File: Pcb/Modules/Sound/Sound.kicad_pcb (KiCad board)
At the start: 2 copper layers, 15 parts, among them J1 JACK_RJ45, U1 MAX4466

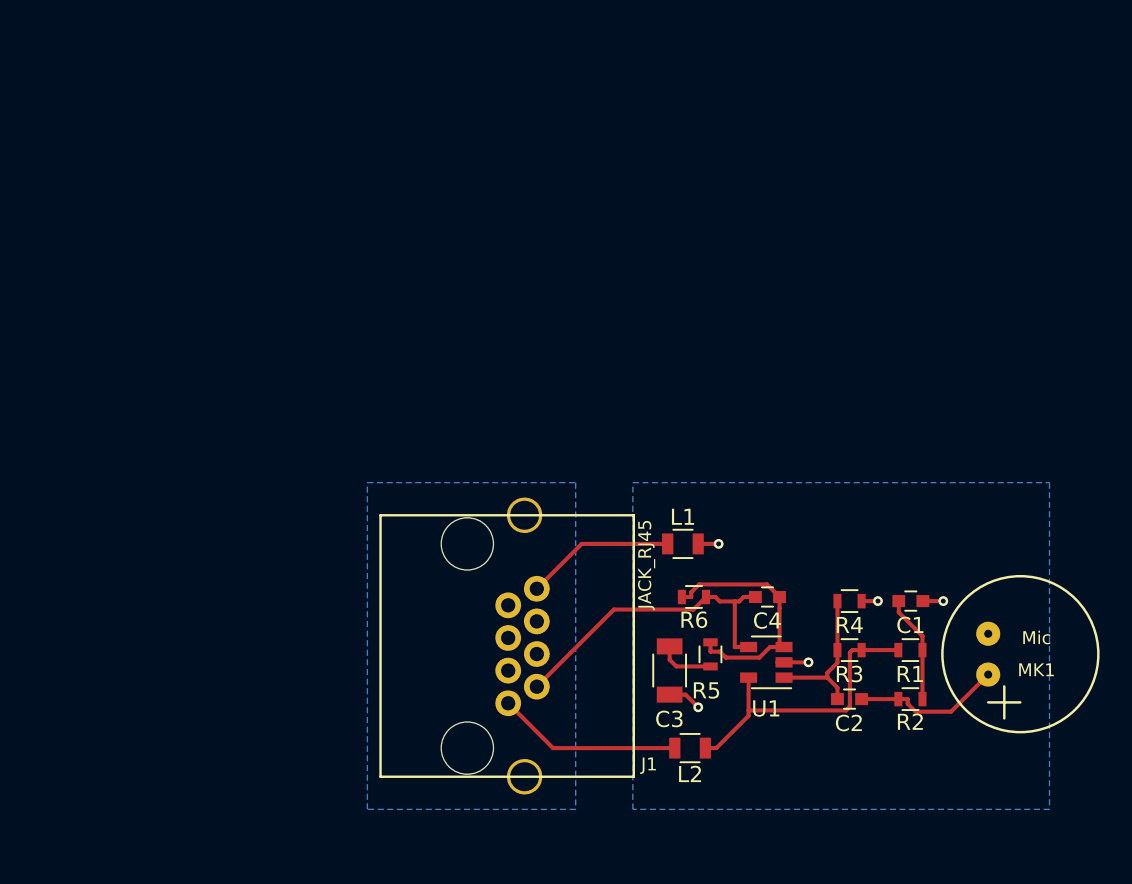
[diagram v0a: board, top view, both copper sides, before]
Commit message: Update module pcbs to common format and fix issues.
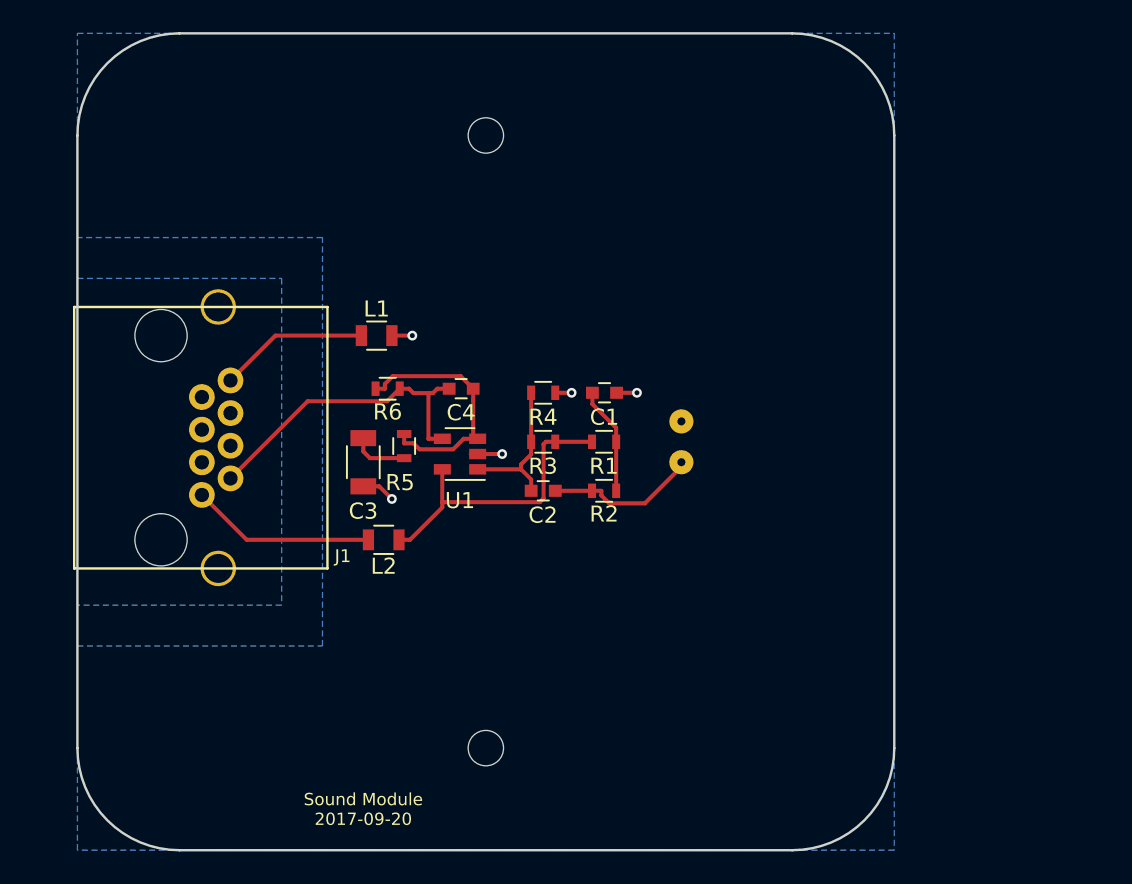
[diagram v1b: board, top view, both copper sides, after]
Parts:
- added REF**: MountingHole_2.2mm_M2, Mounting_Holes:MountingHole_2.2mm_M2, F.Cu at (50.8, 69.8)
- added REF**: MountingHole_2.2mm_M2, Mounting_Holes:MountingHole_2.2mm_M2, F.Cu at (50.8, 31.8)
- MK1: moved to B.Cu
- moved MK1 26.6 mm to (61.0, 50.8), turned to 0 degrees
- moved C2 23.0 mm to (54.4, 53.8)
- moved U1 23.0 mm to (49.2, 51.6)
- moved R3 23.0 mm to (54.4, 50.8)
- moved R4 23.0 mm to (54.4, 47.8)
- moved C1 23.0 mm to (58.2, 47.8)
- moved C3 23.0 mm to (43.2, 52.1)
- moved J1 23.0 mm to (33.0, 50.5)
- moved L1 23.0 mm to (44.0, 44.2)
- moved R2 23.0 mm to (58.2, 53.8)
- moved R6 23.0 mm to (44.7, 47.5)
- moved C4 23.0 mm to (49.3, 47.5)
- moved L2 23.0 mm to (44.5, 56.9)
- moved R1 23.0 mm to (58.2, 50.8)
- moved R5 23.0 mm to (45.7, 51.1)
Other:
- board outline added: 50.8 x 50.8 mm
- net class Default: clearance 0.2032 -> 0.2; trace_width 0.254 -> 0.25; via_dia 0.6096 -> 0.6; via_drill 0.3048 -> 0.4
- rule trace_clearance: 0.2032 -> 0.2
- board text added: "Sound Module 2017-09-20"

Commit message: Update sound module
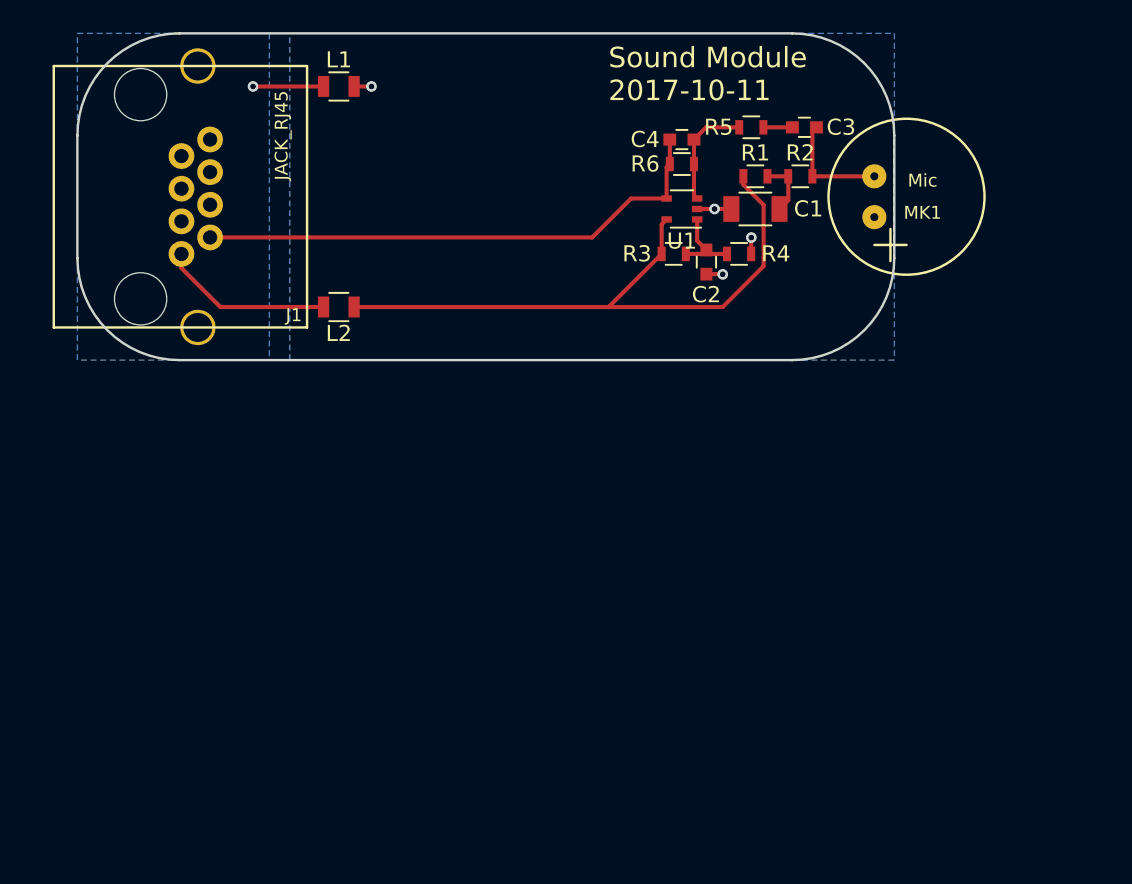
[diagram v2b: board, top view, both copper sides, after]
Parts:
- removed REF** (x2): MountingHole_2.2mm_M2, Mounting_Holes:MountingHole_2.2mm_M2
- C1: value 0.1uF -> 47uF; footprint Capacitors_SMD:C_0603 -> Capacitors_SMD:C_1206
- C2: value 0.01uF -> 1uF
- C3: value 10uF -> 0.1uF; footprint Capacitors_SMD:C_1206 -> Capacitors_SMD:C_0603
- C4: value 100pF -> 47pF
- MK1: moved to F.Cu
- R2: value 1K -> 2.2K
- R3, R4: value 1M -> 100K
- R5: value 1K -> 20K
- R6: value 100K -> 1M
- U1: footprint TO_SOT_Packages_SMD:SOT-23-5 -> TO_SOT_Packages_SMD:SOT-353_SC-70-5
- moved C3 34.4 mm to (70.6, 31.2), turned to 180 degrees
- moved R5 29.3 mm to (67.3, 31.2), turned to 0 degrees
- moved R2 23.1 mm to (70.4, 34.3), turned to 0 degrees
- moved R6 23.0 mm to (63.0, 33.5), turned to 0 degrees
- moved MK1 22.1 mm to (77.0, 35.6), turned to 180 degrees
- moved C4 20.7 mm to (63.0, 32.0)
- moved U1 20.6 mm to (63.0, 36.3)
- moved R1 19.0 mm to (67.6, 34.3)
- moved C2 17.5 mm to (64.5, 39.6), turned to 90 degrees
- moved L1 15.7 mm to (41.7, 28.7)
- moved J1 15.0 mm to (31.8, 35.6)
- moved R4 14.9 mm to (66.5, 39.1)
- moved C1 14.8 mm to (67.6, 36.3), turned to 180 degrees
- moved L2 14.7 mm to (41.7, 42.4)
- moved R3 14.2 mm to (62.5, 39.1), turned to 0 degrees
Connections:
- C2 pad 1: Net-(C2-Pad1) -> GND
- C3 pad 1: GND -> Net-(C3-Pad1)
- MK1 pad 1: GND -> Net-(C3-Pad1)
- MK1 pad 2: Net-(C2-Pad2) -> GND
- R2 pad 2: Net-(C2-Pad2) -> Net-(C3-Pad1)
- R3 pad 2: Net-(C2-Pad1) -> Net-(C2-Pad2)
- R4 pad 1: Net-(C2-Pad1) -> Net-(C2-Pad2)
- U1 pad 1: Net-(C2-Pad1) -> Net-(C2-Pad2)
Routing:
- net +3V3: track 18.7 -> 39.6 mm
- net /AN_VAL: track 19.8 -> 33.1 mm
- net Net-(C2-Pad1): track 9.31 -> 0.00 mm
- net Net-(C4-Pad1): track 15.6 -> 6.88 mm
- net Net-(C3-Pad1): track 0.00 -> 7.01 mm
- net Net-(J1-Pad8): track 9.29 -> 4.38 mm, vias 0 -> 1
- net Net-(C2-Pad2): track 9.32 -> 4.90 mm
- net Net-(C1-Pad1): track 6.71 -> 3.55 mm
- net GND: track 7.61 -> 5.25 mm, vias 5 -> 4
- net Net-(C3-Pad2): track 3.54 -> 1.80 mm
- net Net-(J1-Pad1): track 11.5 -> 10.7 mm
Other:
- board size 50.8 x 50.8 mm -> 50.8 x 20.3 mm
- net class Default: clearance 0.2 -> 0.2032; trace_width 0.25 -> 0.254; via_dia 0.6 -> 0.6604; via_drill 0.4 -> 0.3556
- rule trace_clearance: 0.2 -> 0.2032
- board text added: "Sound Module 2017-10-11"
- board text removed: "Sound Module 2017-09-20"

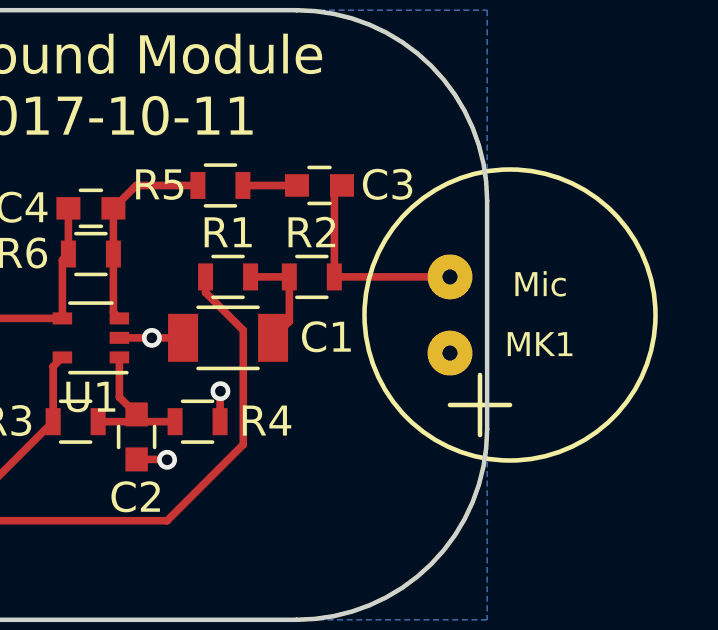
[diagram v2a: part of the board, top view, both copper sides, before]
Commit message: Update vibration module pcb
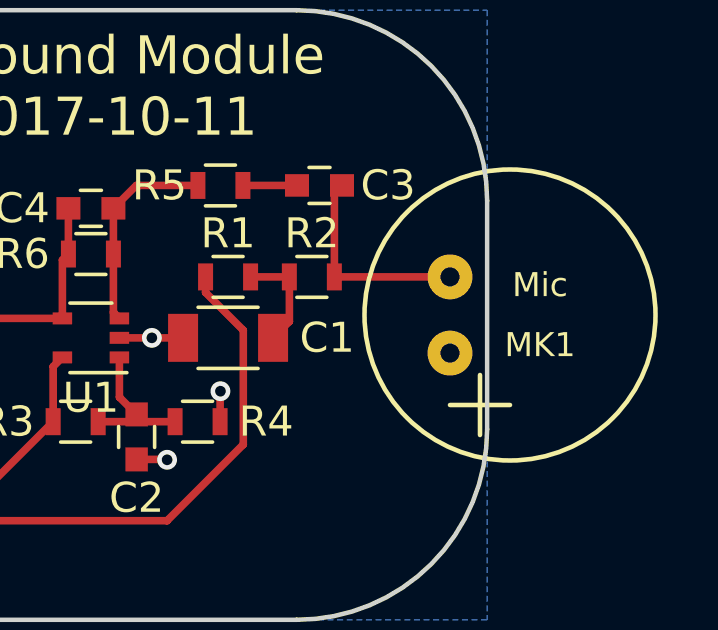
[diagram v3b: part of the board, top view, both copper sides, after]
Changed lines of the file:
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@@
     (links 26)
     (no_connects 0)
-    (area 25.324999 25.324999 76.275001 45.795001)
+    (area 23.651869 25.324999 82.091401 45.795001)
     (thickness 1.6)
     (drawings 9)
@@
     (mod_text_size 1 1)
     (mod_text_width 0.15)
-    (pad_size 1.524 1.524)
-    (pad_drill 0.762)
+    (pad_size 1.5 1.5)
+    (pad_drill 0.635)
     (pad_to_mask_clearance 0.2)
     (aux_axis_origin 0 0)
@@
     (fp_line (start 1 -4) (end 1 -2) (layer F.SilkS) (width 0.1524))
     (fp_circle (center 0 0) (end 4.85 0) (layer F.SilkS) (width 0.1524))
-    (pad 1 thru_hole circle (at 2 1.27 180) (size 1.5 1.5) (drill 0.5) (layers *.Cu *.Mask)
+    (pad 1 thru_hole circle (at 2 1.27 180) (size 1.5 1.5) (drill 0.635) (layers *.Cu *.Mask)
       (net 10 "Net-(C3-Pad1)"))
-    (pad 2 thru_hole circle (at 2 -1.27 180) (size 1.5 1.5) (drill 0.5) (layers *.Cu *.Mask)
+    (pad 2 thru_hole circle (at 2 -1.27 180) (size 1.5 1.5) (drill 0.635) (layers *.Cu *.Mask)
       (net 1 GND))
   )

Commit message: Update Valve module
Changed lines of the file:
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@@
     (add_net "Net-(J1-Pad8)")
-  )
-  (module CA6:MIC_CMA-4544PF (layer F.Cu)
-    (at 76.962 35.56 180)
-    (tags "CMS SM")
-    (attr smd)
-    (fp_text reference MK1 (at -1 -1 180) (layer F.SilkS)
-      (effects (font (size 0.8 0.8) (thickness 0.15)))
-    )
-    (fp_text value Mic (at -1 1 180) (layer F.SilkS)
-      (effects (font (size 0.8 0.8) (thickness 0.15)))
-    )
-    (fp_line (start 0 -3) (end 2 -3) (layer F.SilkS) (width 0.1524))
-    (fp_line (start 1 -4) (end 1 -2) (layer F.SilkS) (width 0.1524))
-    (fp_circle (center 0 0) (end 4.85 0) (layer F.SilkS) (width 0.1524))
-    (pad 1 thru_hole circle (at 2 1.27 180) (size 1.5 1.5) (drill 0.635) (layers *.Cu *.Mask)
-      (net 10 "Net-(C3-Pad1)"))
-    (pad 2 thru_hole circle (at 2 -1.27 180) (size 1.5 1.5) (drill 0.635) (layers *.Cu *.Mask)
-      (net 1 GND))
   )
   (module Capacitors_SMD:C_0603 (layer F.Cu)
@@
     )
   )
+  (module CA6:MIC_CMA-4544PF (layer F.Cu)
+    (at 76.962 35.56 180)
+    (tags "CMS SM")
+    (attr smd)
+    (fp_text reference MK1 (at -1 -1 180) (layer F.SilkS)
+      (effects (font (size 0.8 0.8) (thickness 0.15)))
+    )
+    (fp_text value Mic (at -1 1 180) (layer F.SilkS)
+      (effects (font (size 0.8 0.8) (thickness 0.15)))
+    )
+    (fp_circle (center 0 0) (end 4.85 0) (layer F.SilkS) (width 0.1524))
+    (pad 1 thru_hole circle (at 2 1.27 180) (size 1.5 1.5) (drill 0.635) (layers *.Cu *.Mask)
+      (net 10 "Net-(C3-Pad1)"))
+    (pad 2 thru_hole circle (at 2 -1.27 180) (size 1.5 1.5) (drill 0.635) (layers *.Cu *.Mask)
+      (net 1 GND))
+  )
   (gr_line (start 25.4 31.75) (end 25.4 39.37) (angle 90) (layer Edge.Cuts) (width 0.15))

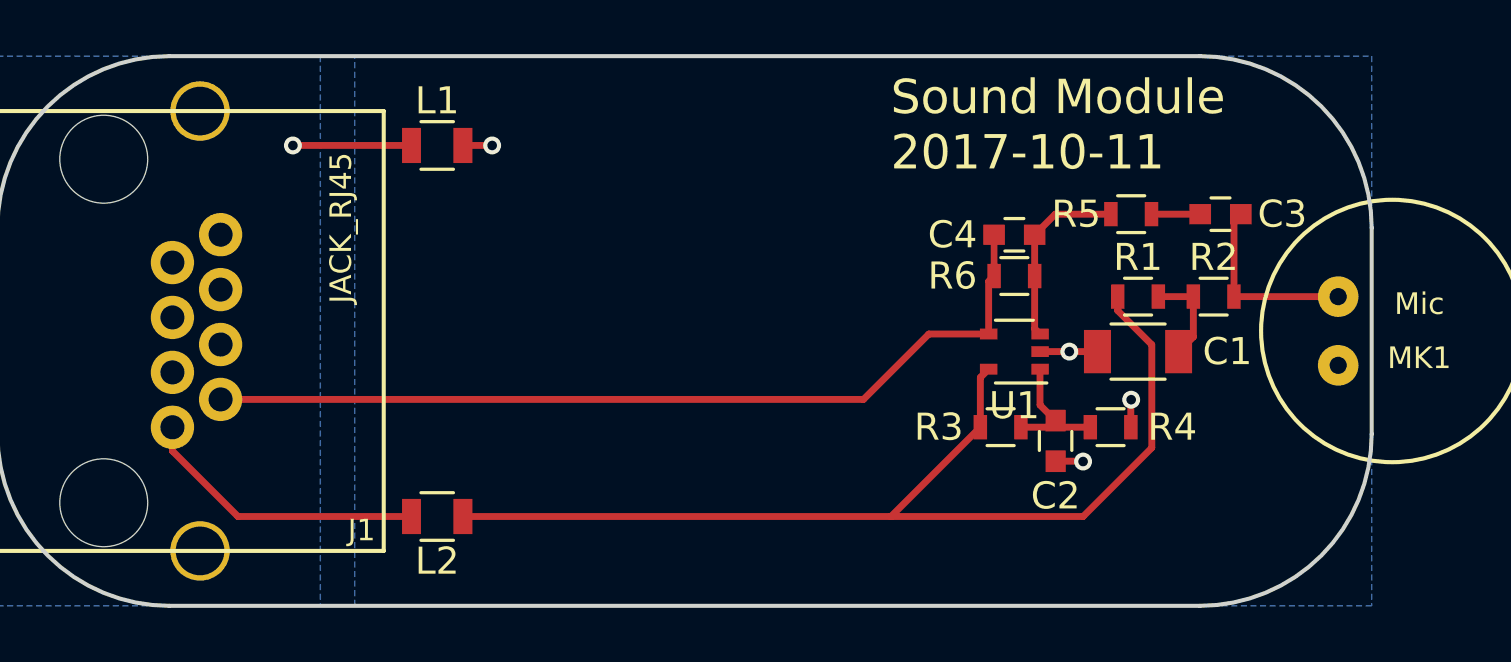
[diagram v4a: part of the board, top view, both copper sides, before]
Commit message: Fix up PCB traces
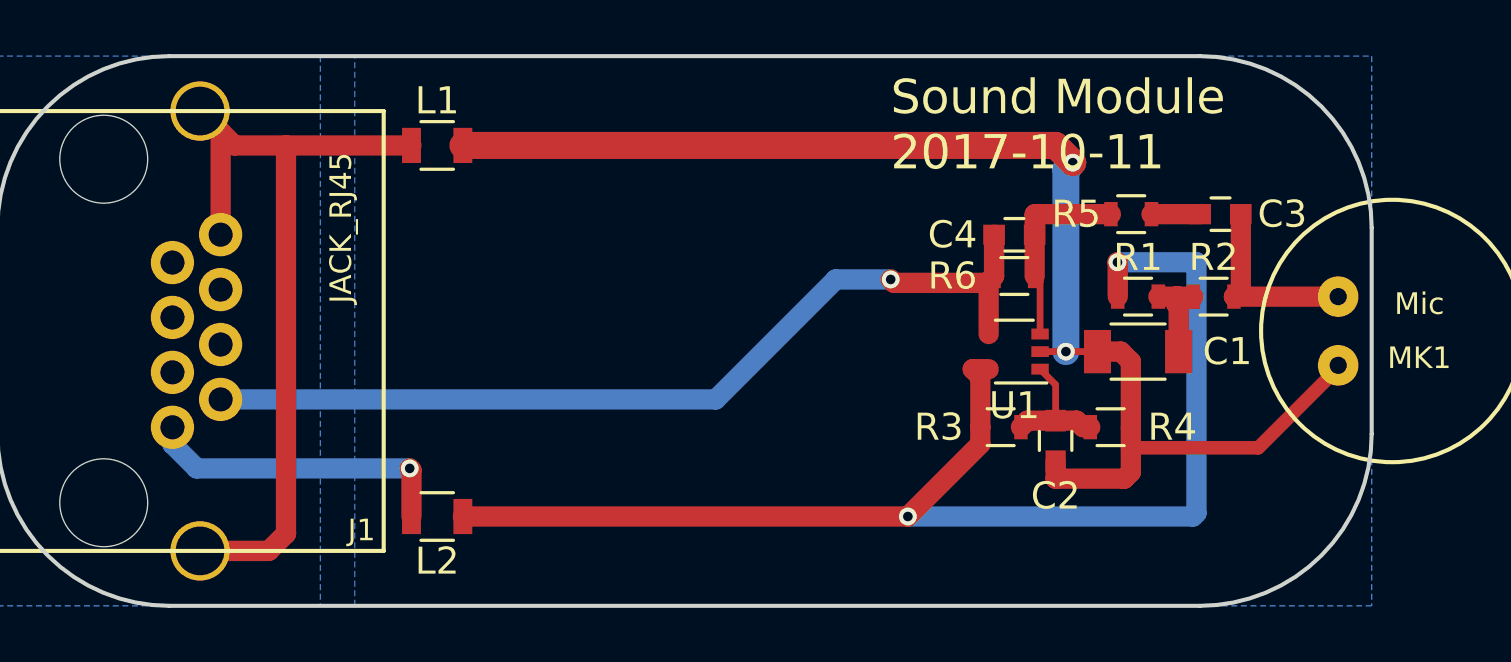
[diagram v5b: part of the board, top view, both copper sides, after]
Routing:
- net GND: track 5.25 -> 50.0 mm, vias 4 -> 2
- net Net-(J1-Pad8): track 4.38 -> 31.0 mm, vias 1 -> 0
- net +3V3: track 39.6 -> 47.9 mm, vias 0 -> 2
- net /AN_VAL: track 33.1 -> 34.4 mm, vias 0 -> 1
- net Net-(J1-Pad1): track 10.7 -> 11.6 mm, vias 0 -> 1
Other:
- net class Default: trace_width 0.254 -> 1
